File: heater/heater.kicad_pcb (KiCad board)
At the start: 2 copper layers, 9 parts, among them J1 power Input, J2 input uC, J3 thermostat, J4 to mcu, Q1 BC517

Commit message: heater done
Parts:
- removed R1: 47, Resistors_THT:R_Axial_DIN0414_L11.9mm_D4.5mm_P15.24mm_Horizontal
- added Q2: BC517, TO_SOT_Packages_THT:TO-92_Inline_Wide, F.Cu at (165.0, 95.6)
- added R5: 1k, Resistors_SMD:R_0805_HandSoldering, F.Cu at (156.0, 96.0)
- added REF***: OSHW-Logo2_14.6x12mm_SilkScreen, Symbols:OSHW-Logo2_14.6x12mm_SilkScreen, F.Cu at (181.8, 88.3)
- J1: footprint Connectors_JST:JST_EH_B04B-EH-A_04x2.50mm_Straight -> Connectors_JST:JST_XH_B04B-XH-A_04x2.50mm_Straight
- J2: value input uC -> MCUpins; footprint Socket_Strips:Socket_Strip_Straight_1x01_Pitch2.54mm -> Connectors_JST:JST_XH_B03B-XH-A_03x2.50mm_Straight
- J3: value thermostat -> thermistor; footprint Socket_Strips:Socket_Strip_Straight_1x02_Pitch2.54mm -> Connectors_JST:JST_XH_B02B-XH-A_02x2.50mm_Straight
- J4: value to mcu -> fan; footprint Socket_Strips:Socket_Strip_Straight_1x01_Pitch2.54mm -> Connectors_JST:JST_XH_B02B-XH-A_02x2.50mm_Straight
- R2: value 10 -> 27; footprint Resistors_THT:R_Axial_Power_L75.0mm_W9.0mm_P81.28mm -> Resistors_THT:R_Axial_Power_L38.0mm_W9.0mm_P40.64mm
- R3, R4: value R_US -> 1k
- moved R2 73.4 mm to (171.4, 95.9), turned to 180 degrees
- moved J4 54.4 mm to (168.8, 86.8)
- moved J2 51.0 mm to (156.4, 86.8)
- moved R3 41.0 mm to (151.0, 96.0), turned to 270 degrees
- moved Q1 36.6 mm to (147.8, 95.5), turned to 180 degrees
- moved J1 33.0 mm to (141.5, 86.8), turned to 0 degrees
- moved J3 22.2 mm to (131.5, 86.8)
- moved R4 20.7 mm to (136.2, 95.5), turned to 90 degrees
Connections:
- J1 pad 1: Net-(J1-Pad1) -> GND
- J1 pad 2: +12V -> +5V
- J1 pad 3: +5V -> +12V
- J1 pad 4: GND -> Net-(J1-Pad4)
- J2 pad 1: Net-(J2-Pad1) -> /fromMcuF
- J3 pad 2: /mcu -> /toMcu
- J4 pad 1: /mcu -> +12V
- R2 pad 2: Net-(R1-Pad1) -> +12V
- R3 pad 2: Net-(J2-Pad1) -> /fromMcuR
- R4 pad 2: /mcu -> /toMcu
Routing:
- net GND: track 0.00 -> 55.3 mm
- net Net-(R1-Pad1): track 48.0 -> 0.00 mm
- net /toMcu: track 0.00 -> 45.2 mm
- net /mcu: track 35.8 -> 0.00 mm
- net +12V: track 21.0 -> 47.2 mm
- net /fromMcuR: track 0.00 -> 20.9 mm
- net Net-(J2-Pad1): track 12.7 -> 0.00 mm
- net Net-(J4-Pad2): track 0.00 -> 12.6 mm
- net Net-(Q2-Pad2): track 0.00 -> 11.9 mm
- net Net-(Q1-Pad1): track 40.3 -> 28.6 mm
- net /fromMcuF: track 0.00 -> 7.97 mm
- net +5V: track 12.5 -> 20.0 mm
- net Net-(Q1-Pad2): track 10.7 -> 8.39 mm
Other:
- board outline added: 80 x 22 mm
- net class +12V added: clearance 0.5, trace_width 1, via_dia 0.8, via_drill 0.4
- board text added: "12V"
- board text added: "5V"
- board text added: "GND"
- board text added: "OpenPLC FOSSEE"
- board text added: "fan"
- board text added: "temp"
- board text added: "toMcu"

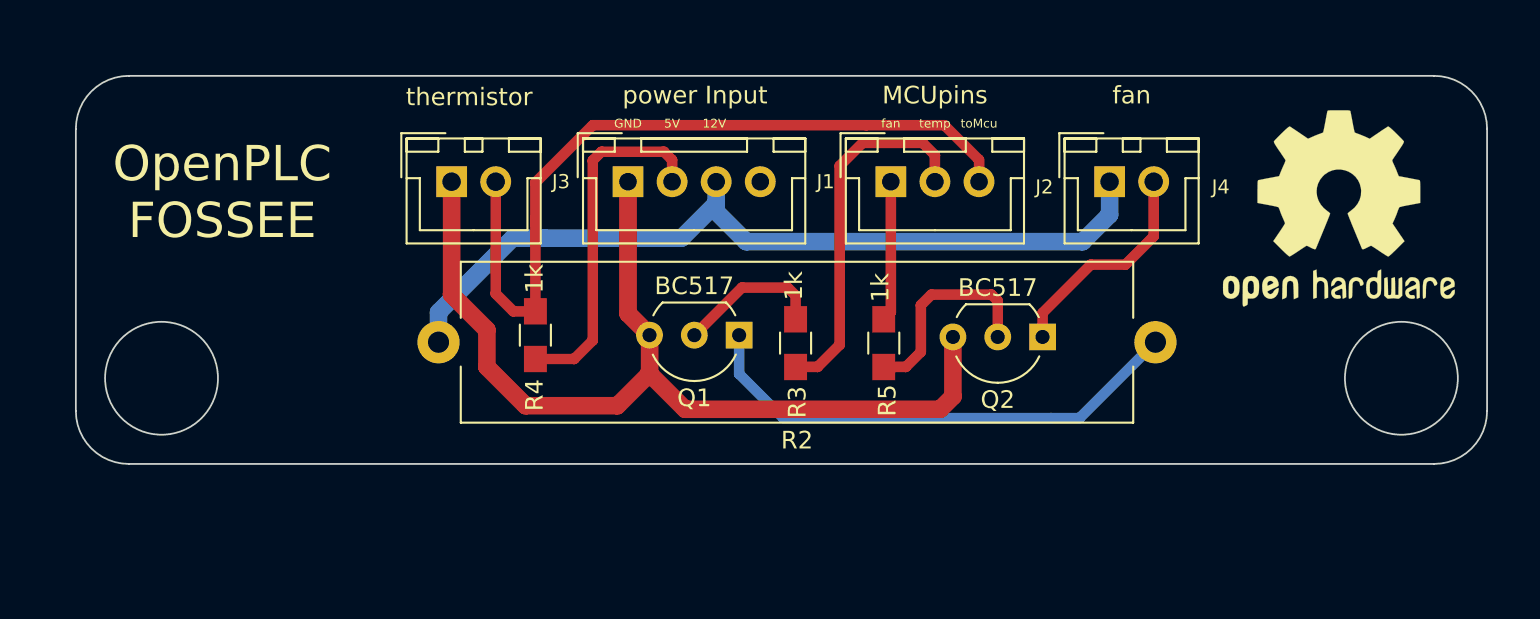
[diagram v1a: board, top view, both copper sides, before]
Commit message: added indicator LED's in heater module; added proper markings in motor module.
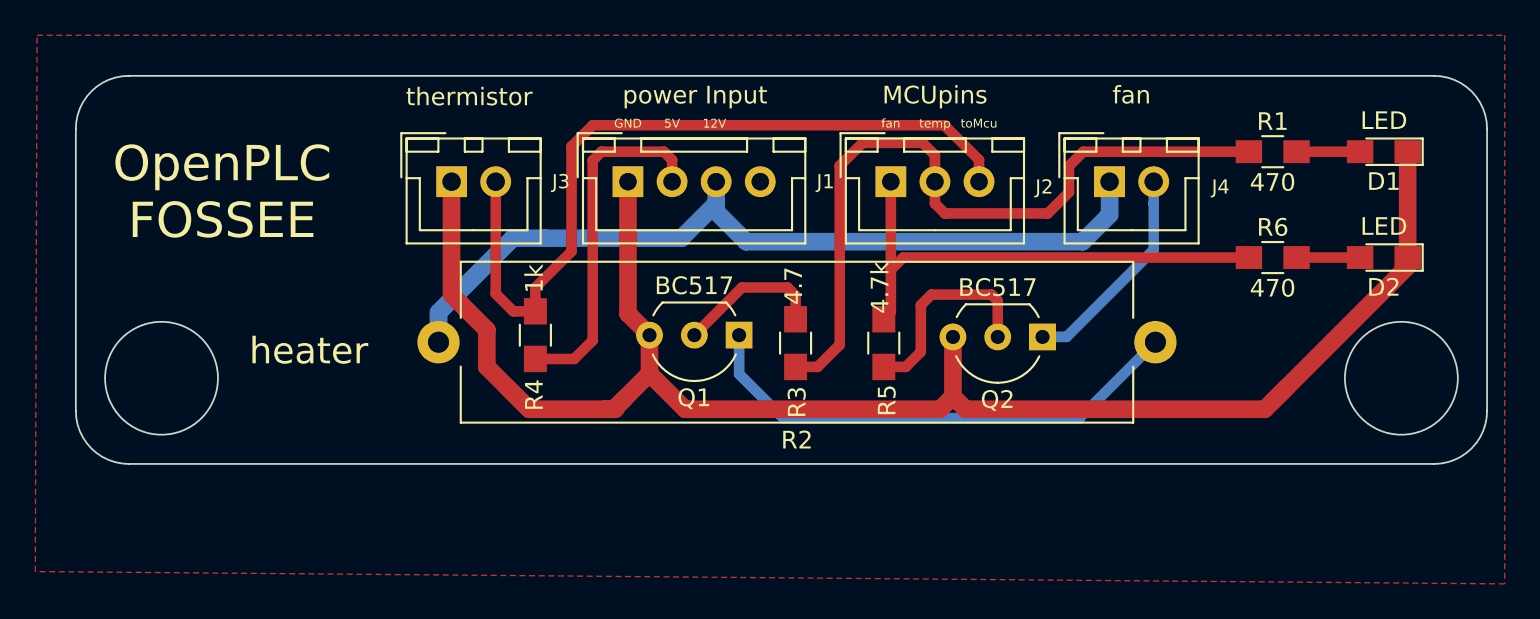
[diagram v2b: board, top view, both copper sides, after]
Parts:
- removed REF***: OSHW-Logo2_14.6x12mm_SilkScreen, Symbols:OSHW-Logo2_14.6x12mm_SilkScreen
- added D1: LED, LEDs:LED_0805_HandSoldering, F.Cu at (184.3, 85.1)
- added D2: LED, LEDs:LED_0805_HandSoldering, F.Cu at (184.3, 91.1)
- added R1: 470, Resistors_SMD:R_0805_HandSoldering, F.Cu at (178.1, 85.1)
- added R6: 470, Resistors_SMD:R_0805_HandSoldering, F.Cu at (178.1, 91.1)
- R3: value 1k -> 4.7
- R5: value 1k -> 4.7k
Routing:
- net GND: track 55.3 -> 95.1 mm
- net /fromMcuR: track 20.9 -> 42.5 mm
- net /fromMcuF: track 7.97 -> 28.6 mm
- net Net-(D2-Pad2): track 0.00 -> 3.60 mm
- net Net-(D1-Pad2): track 0.00 -> 3.60 mm
- added copper zone on F.Cu, net GND
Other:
- board text added: "heater"

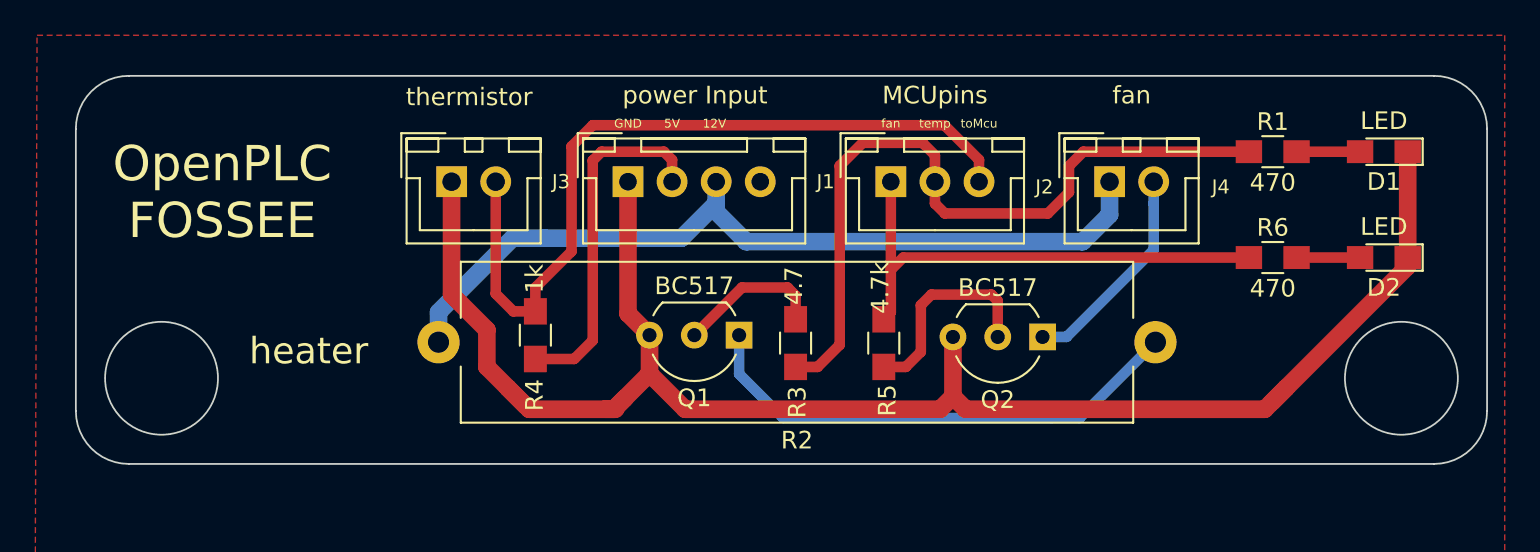
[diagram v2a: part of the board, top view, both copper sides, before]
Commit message: mounting holes in motor, extra pins in traffic, corrections in labels
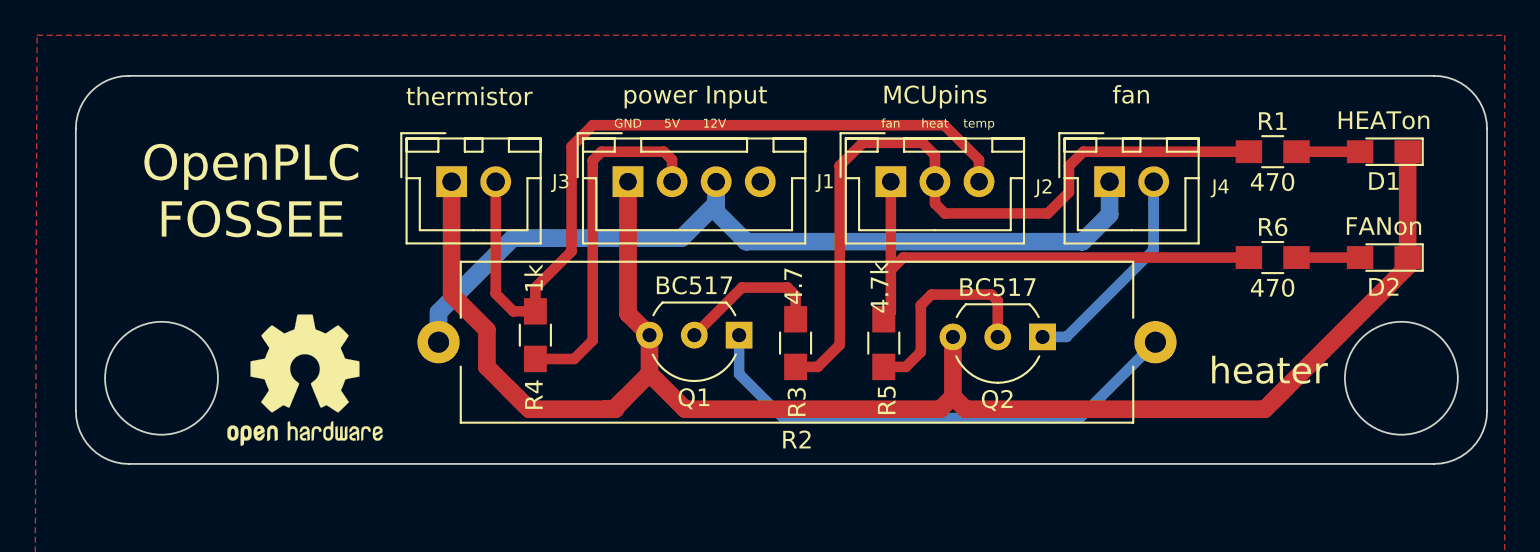
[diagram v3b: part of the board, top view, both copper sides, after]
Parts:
- added REF***: OSHW-Logo2_9.8x8mm_SilkScreen, Symbols:OSHW-Logo2_9.8x8mm_SilkScreen, F.Cu at (123.2, 98.0)
- D1: value LED -> HEATon
- D2: value LED -> FANon
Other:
- board text added: "heat"
- board text removed: "toMcu"
